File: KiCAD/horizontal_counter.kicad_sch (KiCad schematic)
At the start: 14 parts, among them U1 74HC161, U10 74HC04, U11 74HC112, U12 74HC32, U13 74HC173, U14 74HC173, U2 74HC161, U3 74HC161, U4 74HC04, U5 74HC04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

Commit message: assigned footprints
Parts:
- removed unit 4 of U12
- removed unit 3 of U12
- removed unit 1 of U4
- added unit 3 of U10
- added unit 7 of U10
- added unit 2 of U10
- added unit 5 of U5
- added unit 6 of U5
- U1: footprint (none) -> Package_DIP:DIP-16_W7.62mm_LongPads
- U10, U12, U4, U5, U6, U7, U8, U9: footprint (none) -> Package_DIP:DIP-14_W7.62mm
- U11, U13, U14, U2, U3: footprint (none) -> Package_DIP:DIP-16_W7.62mm
- U4: renamed from U5; footprint (none) -> Package_DIP:DIP-14_W7.62mm
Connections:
- net +5V: now also U10.14 (VCC)
- net GND: now also U10.7 (GND)
- net bit_0: no longer U14.14 (D0)
- net bit_1: no longer U14.13 (D1)
- net bit_2: no longer U14.12 (D2)
- net bit_3: no longer U14.11 (D3)
- net bit_4: now also U14.14 (D0)
- net bit_5: now also U14.13 (D1)
- net bit_6: now also U14.12 (D2), U5.1; no longer U10.1
- net bit_7: now also U14.11 (D3)
- net eo_fporch_210: now also U10.2; no longer U8.8
- net eo_line: now also U10.5, U5.10; no longer U6.8
- net eo_syncp_242: now also U10.4; no longer U7.8
- net eo_vis_200: now also U5.12; no longer U11.11 (J), U11.12 (K), U9.8
- net ~{bit_6}: now also U5.2; no longer U10.2
- net ~{rst}: now also U1.1 (~{MR}), U2.1 (~{MR}), U3.1 (~{MR})
- net j_addr4 renamed i_addr4
- net j_addr5 renamed i_addr5
- net j_addr6 renamed i_addr6
- net j_addr7 renamed i_addr7
- new net: U5.11, U6.8
- new net: U10.1, U8.8
- new net: U5.13, U9.8
- new net: U11.11 (J), U11.12 (K)
- new net: U10.3, U7.8
- new net ~{eo_line}: U10.6
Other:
- moved on the sheet: U12A, U5A

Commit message: finished most of the schematics of submodules except DAC, need to work on integration
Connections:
- net eo_vis_200: now also U11.11 (J), U11.12 (K)
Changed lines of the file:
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@@
+	)
+	(junction
+		(at 144.78 105.41)
+		(diameter 0)
+		(color 0 0 0 0)
 	)
 	(junction
@@
 		)
 		(stroke
+			(width 0)
+			(type default)
+		)
+	)
+	(wire
+		(pts
+			(xy 109.22 105.41) (xy 144.78 105.41)
+		)
+		(stroke

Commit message: finished schematics and footprint assignments; need to figure out +5v connection issue
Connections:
- net i_addr4 renamed j_addr4
- net i_addr5 renamed j_addr5
- net i_addr6 renamed j_addr6
- net i_addr7 renamed j_addr7
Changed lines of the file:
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@@
 		)
 	)
-	(label "i_addr5"
+	(label "j_addr5"
 		(at 238.76 163.83 0)
 		(effects
@@
 		)
 	)
-	(label "i_addr1"
+	(label "j_addr1"
 		(at 241.3 104.14 0)
 		(effects
@@
 		)
 	)
-	(label "i_addr0"
+	(label "j_addr0"
 		(at 241.3 101.6 0)
 		(effects
@@
 		)
 	)
-	(label "i_addr6"
+	(label "j_addr6"
 		(at 238.76 166.37 0)
 		(effects
@@
 		)
 	)
-	(label "i_addr2"
+	(label "j_addr2"
 		(at 241.3 106.68 0)
 		(effects
@@
 		)
 	)
-	(label "i_addr4"
+	(label "j_addr4"
 		(at 238.76 161.29 0)
 		(effects
@@
 		)
 	)
-	(label "i_addr3"
+	(label "j_addr3"
 		(at 241.3 109.22 0)
 		(effects
@@
 		)
 	)
-	(label "i_addr7"
+	(label "j_addr7"
 		(at 238.76 168.91 0)
 		(effects
@@
 		)
 	)
-	(hierarchical_label "i_addr[0..7]"
+	(hierarchical_label "j_addr[0..7]"
 		(shape output)
 		(at 284.48 171.45 0)

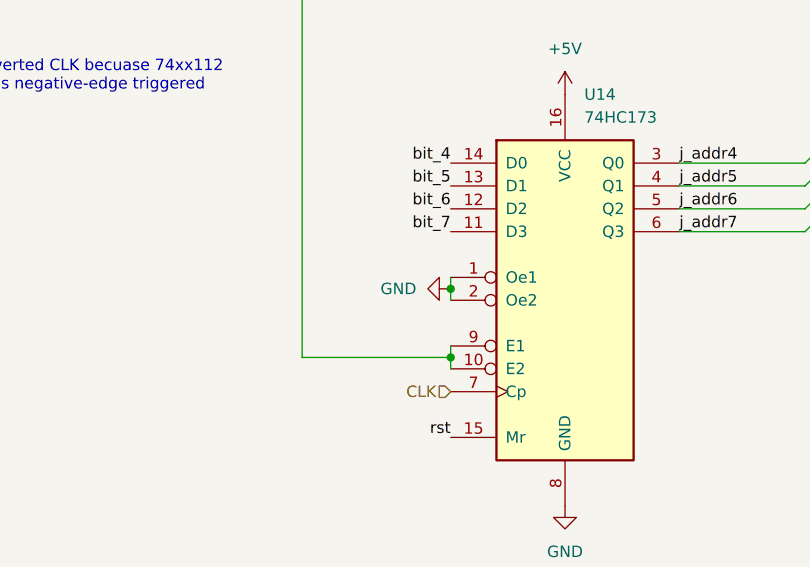
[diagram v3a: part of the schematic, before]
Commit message: fix footprint
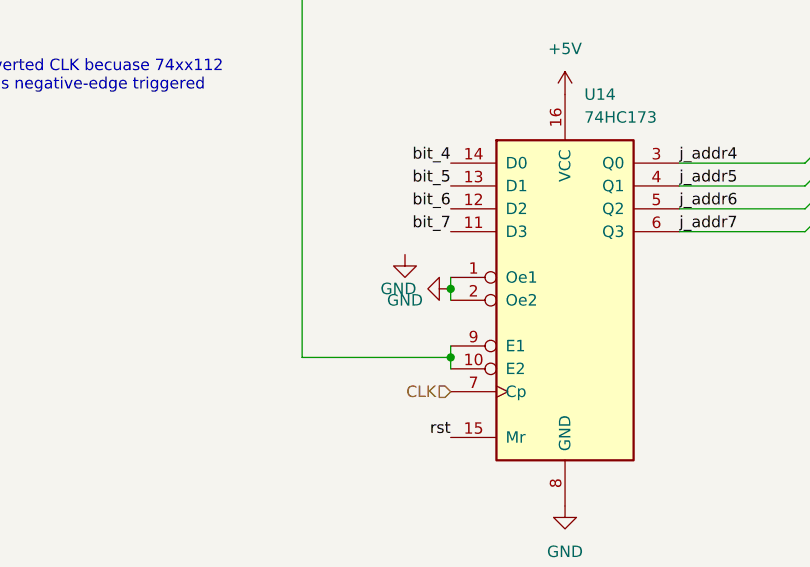
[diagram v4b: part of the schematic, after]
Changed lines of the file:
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@@
+	)
+	(symbol
+		(lib_id "power:GND")
+		(at 208.28 171.45 0)
+		(unit 1)
+		(exclude_from_sim no)
+		(in_bom yes)
+		(on_board yes)
+		(dnp no)
+		(fields_autoplaced yes)
+		(property "Reference" "#PWR0119"
+			(at 208.28 177.8 0)
+			(effects
+				(font
+					(size 1.27 1.27)
+				)
+				(hide yes)
+			)
+		)
+		(property "Value" "GND"
+			(at 208.28 176.53 0)
+			(effects
+				(font
+					(size 1.27 1.27)
+				)
+			)
+		)
+		(property "Footprint" ""
+			(at 208.28 171.45 0)
+			(effects
+				(font
+					(size 1.27 1.27)
+				)
+				(hide yes)
+			)
+		)
+		(property "Datasheet" ""
+			(at 208.28 171.45 0)
+			(effects
+				(font
+					(size 1.27 1.27)
+				)
+				(hide yes)
+			)
+		)
+		(property "Description" "Power symbol creates a global label with name \"GND\" , ground"
+			(at 208.28 171.45 0)
+			(effects
+				(font
+					(size 1.27 1.27)
+				)
+				(hide yes)
+			)
+		)
+		(pin "1"
+		)
+		(instances
+			(project ""
+				(path "/53ebbfbe-eaa1-4706-acc1-611a99db7179/702d4f80-011b-486e-94b5-09c5f3eee61f"
+					(reference "#PWR0119")
+					(unit 1)
+				)
+			)
+		)
 	)
 	(symbol

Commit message: update pcb
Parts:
- U1: footprint Package_DIP:DIP-16_W7.62mm_LongPads -> Package_DIP:DIP-16_W7.62mm
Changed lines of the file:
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@@
 			)
 		)
-		(property "Footprint" "Package_DIP:DIP-16_W7.62mm_LongPads"
+		(property "Footprint" "Package_DIP:DIP-16_W7.62mm"
 			(at 43.18 49.53 0)
 			(effects

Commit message: fix multiple ERCs that made RAM addrs not connecting
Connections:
- no-connect marks 3 -> 8
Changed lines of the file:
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@@
 	)
 	(no_connect
+		(at 146.05 49.53)
+	)
+	(no_connect
+		(at 146.05 44.45)
+	)
+	(no_connect
 		(at 148.59 104.14)
 	)
 	(no_connect
+		(at 162.56 144.78)
+	)
+	(no_connect
+		(at 146.05 39.37)
+	)
+	(no_connect
 		(at 144.78 107.95)
 	)
@@
 		(at 144.78 142.24)
 	)
+	(no_connect
+		(at 146.05 41.91)
+	)
 	(bus_entry
 		(at 255.27 163.83)
@@
 					(unit 1)
 				)
-			)
-		)
-	)
-	(symbol
-		(lib_id "power:GND")
-		(at 208.28 171.45 0)
-		(unit 1)
-		(exclude_from_sim no)
-		(in_bom yes)
-		(on_board yes)
-		(dnp no)
-		(fields_autoplaced yes)
-		(property "Reference" "#PWR0119"
-			(at 208.28 177.8 0)
-			(effects
-				(font
-					(size 1.27 1.27)
-				)
-				(hide yes)
-			)
-		)
-		(property "Value" "GND"
-			(at 208.28 176.53 0)
-			(effects
-				(font
-					(size 1.27 1.27)
-				)
-			)
-		)
-		(property "Footprint" ""
-			(at 208.28 171.45 0)
-			(effects
-				(font
-					(size 1.27 1.27)
-				)
-				(hide yes)
-			)
-		)
-		(property "Datasheet" ""
-			(at 208.28 171.45 0)
-			(effects
-				(font
-					(size 1.27 1.27)
-				)
-				(hide yes)
-			)
-		)
-		(property "Description" "Power symbol creates a global label with name \"GND\" , ground"
-			(at 208.28 171.45 0)
-			(effects
-				(font
-					(size 1.27 1.27)
-				)
-				(hide yes)
-			)
-		)
-		(pin "1"
-		)
-		(instances
-			(project ""
-				(path "/53ebbfbe-eaa1-4706-acc1-611a99db7179/702d4f80-011b-486e-94b5-09c5f3eee61f"
-					(reference "#PWR0119")
-					(unit 1)
-				)

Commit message: resolve ERCs for addr combiner
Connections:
- no-connect marks 8 -> 5
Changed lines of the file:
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@@
-	)
-	(no_connect
-		(at 148.59 104.14)
 	)
 	(no_connect
@@
 	)
 	(no_connect
-		(at 144.78 107.95)
-	)
-	(no_connect
-		(at 144.78 142.24)
-	)
-	(no_connect

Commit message: clean up; resolve ERC warnings
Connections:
- net j_addr0: now also U13.3 (Q0)
- net j_addr1: now also U13.4 (Q1)
- net j_addr2: now also U13.5 (Q2)
- net j_addr3: now also U13.6 (Q3)
